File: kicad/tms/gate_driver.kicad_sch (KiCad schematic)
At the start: 12 parts, among them T2 Transformer_1P_1S, U4 L7812, U5 TC4420, U6 NSL-32

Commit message: Kicad files
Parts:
- removed C4: 0.33μF, symbol Device:C
- removed C5: 0.1μF, symbol Device:C
- removed U4: L7812, symbol Regulator_Linear:L7812
- T2: value Transformer_1P_1S -> P0584NL
- U5: renamed from U6; value NSL-32 -> VO2611
- renumbered C9 to C8, C6 to C9, R11 to R18, R12 to R19, U5 to U6
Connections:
- net PSU 12V: now reaches C8.1, C9.1, U6.1 (VDD), U6.8 (VDD)
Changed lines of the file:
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@@
     (title "Gate Driver Circuit")
   )
-  (junction (at 106.68 95.25) (diameter 0) (color 0 0 0 0)
-  )
-  (junction (at 115.57 87.63) (diameter 0) (color 0 0 0 0)
-  )
-  (junction (at 97.79 87.63) (diameter 0) (color 0 0 0 0)
-  )
   (junction (at 207.01 96.52) (diameter 0) (color 0 0 0 0)
   )
@@
     (stroke (width 0) (type default))
   )
-  (wire (pts (xy 97.79 95.25) (xy 106.68 95.25))
-    (stroke (width 0) (type default))
-  )
   (wire (pts (xy 130.81 109.22) (xy 116.84 109.22))
     (stroke (width 0) (type default))
@@
     (stroke (width 0) (type default))
   )
-  (wire (pts (xy 83.82 87.63) (xy 97.79 87.63))
-    (stroke (width 0) (type default))
-  )
   (wire (pts (xy 158.75 87.63) (xy 157.48 87.63))
     (stroke (width 0) (type default))
   )
-  (wire (pts (xy 114.3 87.63) (xy 115.57 87.63))
-    (stroke (width 0) (type default))
-  )
   (wire (pts (xy 207.01 97.79) (xy 207.01 96.52))
     (stroke (width 0) (type default))
   )
-  (wire (pts (xy 106.68 95.25) (xy 115.57 95.25))
-    (stroke (width 0) (type default))
-  )
-  (wire (pts (xy 97.79 87.63) (xy 99.06 87.63))
-    (stroke (width 0) (type default))
-  )
   (wire (pts (xy 158.75 87.63) (xy 158.75 104.14))
     (stroke (width 0) (type default))
@@
     (stroke (width 0) (type default))
   )
-  (wire (pts (xy 115.57 87.63) (xy 143.51 87.63))
+  (wire (pts (xy 135.89 87.63) (xy 143.51 87.63))
     (stroke (width 0) (type default))
   )
@@
     )
   )
-  (global_label "PSU 24V" (shape input) (at 83.82 87.63 180) (fields_autoplaced)
+  (global_label "PSU 12V" (shape input) (at 135.89 87.63 180) (fields_autoplaced)
     (effects (font (size 1.27 1.27)) (justify right))
-    (property "Intersheetrefs" "${INTERSHEET_REFS}" (at 72.5496 87.63 0)
+    (property "Intersheetrefs" "${INTERSHEET_REFS}" (at 124.6196 87.63 0)
       (effects (font (size 1.27 1.27)) (justify right) hide)
     )
@@
     )
   )
-  (symbol (lib_id "Device:C") (at 97.79 91.44 0) (mirror y) (unit 1)
-    (in_bom yes) (on_board yes) (dnp no)
-    (property "Reference" "C4" (at 93.98 90.17 0)
-      (effects (font (size 1.27 1.27)) (justify left))
-    )
-    (property "Value" "0.33μF" (at 93.98 92.71 0)
-      (effects (font (size 1.27 1.27)) (justify left))
-    )
-    (property "Footprint" "" (at 96.8248 95.25 0)
-      (effects (font (size 1.27 1.27)) hide)
-    )
-    (property "Datasheet" "~" (at 97.79 91.44 0)
-      (effects (font (size 1.27 1.27)) hide)
-    )
-    (pin "1")
-    (pin "2")
-    (instances
-      (project "tms"
-        (path "/dc88686f-c772-4c63-b1cc-83a281c6b46c/025e288f-ab42-4019-86f4-e6a324d46d8a"
-          (reference "C4") (unit 1)
-        )
-      )
-    )
-  )
   (symbol (lib_id "power:+5V") (at 97.79 109.22 0) (unit 1)
     (in_bom yes) (on_board yes) (dnp no)
@@
         (path "/dc88686f-c772-4c63-b1cc-83a281c6b46c/025e288f-ab42-4019-86f4-e6a324d46d8a"
           (reference "#PWR011") (unit 1)
-        )
-      )
-    )
-  )
-  (symbol (lib_id "Regulator_Linear:L7812") (at 106.68 87.63 0) (unit 1)
-    (in_bom yes) (on_board yes) (dnp no) (fields_autoplaced)
-    (property "Reference" "U4" (at 106.68 81.28 0)
-      (effects (font (size 1.27 1.27)))
-    )
-    (property "Value" "L7812" (at 106.68 83.82 0)
-      (effects (font (size 1.27 1.27)))
-    )
-    (property "Footprint" "" (at 107.315 91.44 0)
-      (effects (font (size 1.27 1.27) italic) (justify left) hide)
-    )
-    (property "Datasheet" "http://www.st.com/content/ccc/resource/technical/document/datasheet/41/4f/b3/b0/12/d4/47/88/CD00000444.pdf/files/CD00000444.pdf/jcr:content/translations/en.CD00000444.pdf" (at 106.68 88.9 0)
-      (effects (font (size 1.27 1.27)) hide)
-    )
-    (pin "1")
-    (pin "3")
-    (pin "2")
-    (instances
-      (project "tms"
-        (path "/dc88686f-c772-4c63-b1cc-83a281c6b46c/025e288f-ab42-4019-86f4-e6a324d46d8a"
-          (reference "U4") (unit 1)
         )
       )
@@
     )
   )
-  (symbol (lib_id "power:GND") (at 106.68 95.25 0) (unit 1)
-    (in_bom yes) (on_board yes) (dnp no) (fields_autoplaced)
-    (property "Reference" "#PWR09" (at 106.68 101.6 0)
-      (effects (font (size 1.27 1.27)) hide)
-    )
-    (property "Value" "GND" (at 106.68 100.33 0)
-      (effects (font (size 1.27 1.27)))
-    )
-    (property "Footprint" "" (at 106.68 95.25 0)
-      (effects (font (size 1.27 1.27)) hide)
-    )
-    (property "Datasheet" "" (at 106.68 95.25 0)
-      (effects (font (size 1.27 1.27)) hide)
-    )
-    (pin "1")
-    (instances
-      (project "tms"
-        (path "/dc88686f-c772-4c63-b1cc-83a281c6b46c/025e288f-ab42-4019-86f4-e6a324d46d8a"
-          (reference "#PWR09") (unit 1)
-        )
-      )
-    )
-  )
   (symbol (lib_id "Isolator:NSL-32") (at 114.3 116.84 90) (unit 1)
     (in_bom yes) (on_board yes) (dnp no) (fields_autoplaced)
-    (property "Reference" "U6" (at 119.38 115.57 90)
+    (property "Reference" "U5" (at 119.38 115.57 90)
       (effects (font (size 1.27 1.27)) (justify right))
     )
-    (property "Value" "NSL-32" (at 119.38 118.11 90)
+    (property "Value" "VO2611" (at 119.38 118.11 90)
       (effects (font (size 1.27 1.27)) (justify right))
     )
@@
       (project "tms"
         (path "/dc88686f-c772-4c63-b1cc-83a281c6b46c/025e288f-ab42-4019-86f4-e6a324d46d8a"
-          (reference "U6") (unit 1)
+          (reference "U5") (unit 1)
         )
       )
@@
   (symbol (lib_id "Device:R") (at 104.14 109.22 90) (mirror x) (unit 1)
     (in_bom yes) (on_board yes) (dnp no)
-    (property "Reference" "R11" (at 104.14 115.57 90)
+    (property "Reference" "R18" (at 104.14 115.57 90)
       (effects (font (size 1.27 1.27)))
     )
@@
       (project "tms"
         (path "/dc88686f-c772-4c63-b1cc-83a281c6b46c/025e288f-ab42-4019-86f4-e6a324d46d8a"
-          (reference "R11") (unit 1)
+          (reference "R18") (unit 1)
         )
       )
@@
   (symbol (lib_id "Device:C") (at 153.67 87.63 90) (unit 1)
     (in_bom yes) (on_board yes) (dnp no)
-    (property "Reference" "C6" (at 153.67 81.28 90)
+    (property "Reference" "C9" (at 153.67 81.28 90)
       (effects (font (size 1.27 1.27)))
     )
@@
       (project "tms"
         (path "/dc88686f-c772-4c63-b1cc-83a281c6b46c/025e288f-ab42-4019-86f4-e6a324d46d8a"
-          (reference "C6") (unit 1)
+          (reference "C9") (unit 1)
         )
       )
@@
     )
   )
-  (symbol (lib_id "Device:C") (at 115.57 91.44 0) (unit 1)
-    (in_bom yes) (on_board yes) (dnp no)
-    (property "Reference" "C5" (at 119.38 90.17 0)
-      (effects (font (size 1.27 1.27)) (justify left))
-    )
-    (property "Value" "0.1μF" (at 119.38 92.71 0)
-      (effects (font (size 1.27 1.27)) (justify left))
-    )
-    (property "Footprint" "" (at 116.5352 95.25 0)
-      (effects (font (size 1.27 1.27)) hide)
-    )
-    (property "Datasheet" "~" (at 115.57 91.44 0)
-      (effects (font (size 1.27 1.27)) hide)
-    )
-    (pin "1")
-    (pin "2")
-    (instances
-      (project "tms"
-        (path "/dc88686f-c772-4c63-b1cc-83a281c6b46c/025e288f-ab42-4019-86f4-e6a324d46d8a"
-          (reference "C5") (unit 1)
-        )
-      )
-    )
-  )
   (symbol (lib_id "power:GND") (at 143.51 104.14 0) (unit 1)
     (in_bom yes) (on_board yes) (dnp no) (fields_autoplaced)
@@
   (symbol (lib_id "Device:C") (at 153.67 76.2 90) (unit 1)
     (in_bom yes) (on_board yes) (dnp no)
-    (property "Reference" "C9" (at 153.67 69.85 90)
+    (property "Reference" "C8" (at 153.67 69.85 90)
       (effects (font (size 1.27 1.27)))
     )
@@
       (project "tms"
         (path "/dc88686f-c772-4c63-b1cc-83a281c6b46c/025e288f-ab42-4019-86f4-e6a324d46d8a"
-          (reference "C9") (unit 1)
+          (reference "C8") (unit 1)
         )
       )
@@
   (symbol (lib_id "Driver_FET:TC4422") (at 143.51 96.52 0) (unit 1)
     (in_bom yes) (on_board yes) (dnp no)
-    (property "Reference" "U5" (at 143.51 83.82 0)
+    (property "Reference" "U6" (at 143.51 83.82 0)
       (effects (font (size 1.27 1.27)))
     )
@@
       (project "tms"
         (path "/dc88686f-c772-4c63-b1cc-83a281c6b46c/025e288f-ab42-4019-86f4-e6a324d46d8a"
-          (reference "U5") (unit 1)
+          (reference "U6") (unit 1)
         )
       )
@@
   (symbol (lib_id "Device:R") (at 199.39 96.52 90) (unit 1)
     (in_bom yes) (on_board yes) (dnp no) (fields_autoplaced)
-    (property "Reference" "R12" (at 199.39 90.17 90)
+    (property "Reference" "R19" (at 199.39 90.17 90)
       (effects (font (size 1.27 1.27)))
     )
@@
       (project "tms"
         (path "/dc88686f-c772-4c63-b1cc-83a281c6b46c/025e288f-ab42-4019-86f4-e6a324d46d8a"
-          (reference "R12") (unit 1)
+          (reference "R19") (unit 1)
         )
       )
@@
       (effects (font (size 1.27 1.27)))
     )
-    (property "Value" "Transformer_1P_1S" (at 172.7327 93.98 0)
-      (effects (font (size 1.27 1.27)))
-    )
+    (property "Value" "P0584NL" (at 172.7327 93.98 0)
+      (effects (font (size 1.27 1.27)))
+    )

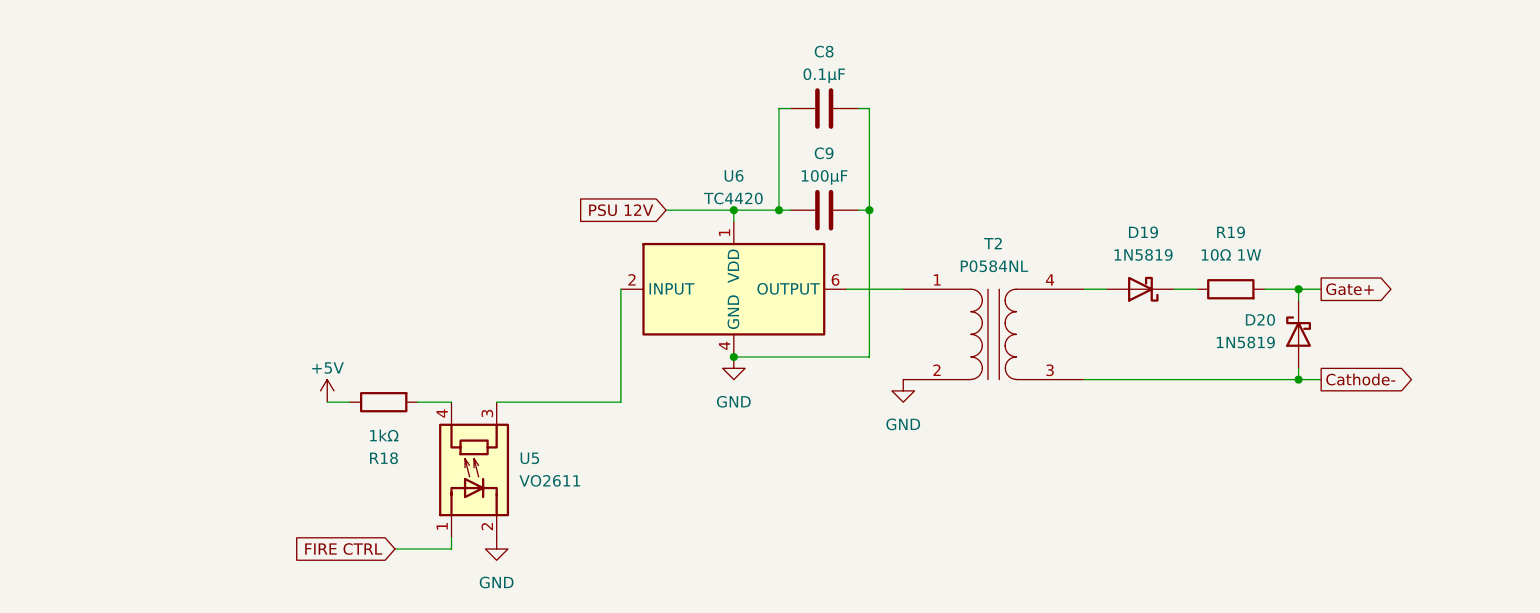
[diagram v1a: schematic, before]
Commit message: Schematic fixes after real life tests
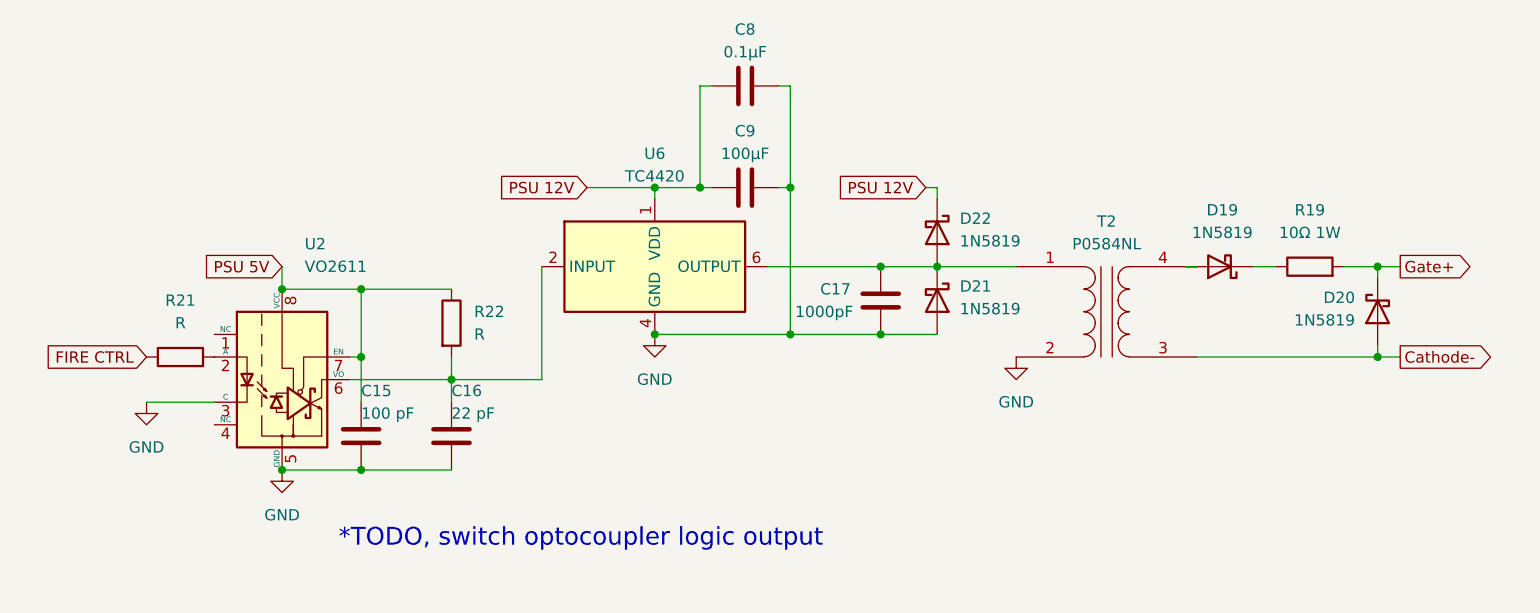
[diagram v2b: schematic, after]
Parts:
- removed R18: 1kΩ, symbol Device:R
- removed U5: VO2611, OptoDevice:Luna_NSL-32, symbol Isolator:NSL-32
- added C15: 100 pF, symbol Device:C
- added C16: 22 pF, symbol Device:C
- added C17: 1000pF, symbol Device:C
- added D21, D22: 1N5819, symbol Device:D_Schottky
- added R21, R22: R, symbol Device:R
- added U2: VO2611, Package_DIP:DIP-8_W7.62mm, symbol Isolator:VO2611
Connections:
- net FIRE CTRL: now also R21.1
- net GND: now also C15.2, C16.2, C17.2, D21.2 (A), U2.3 (C), U2.5 (GND)
- net PSU 12V: now also D22.1 (K)
- net at U6.2 (INPUT): now also C16.1, R22.2, U2.6 (VO)
- net at T2.1 (AA), U6.6 (OUTPUT), U6.7 (OUTPUT): now also C17.1, D21.1 (K), D22.2 (A)
- new net: R21.2, U2.2 (A)
- new net PSU 5V: C15.1, R22.1, U2.7 (EN), U2.8 (VCC)
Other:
- note added: "*TODO, switch optocoupler logic output"
- moved on the sheet: C8, C9, D19, D20, R19, T2, U6

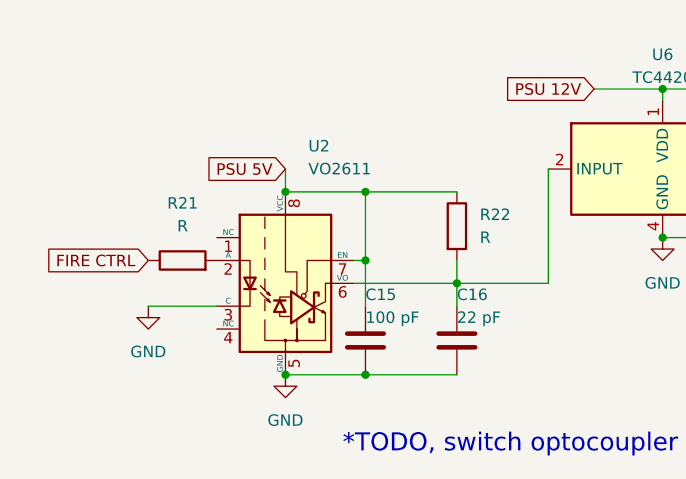
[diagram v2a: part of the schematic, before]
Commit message: Fixed optocoupler output logic
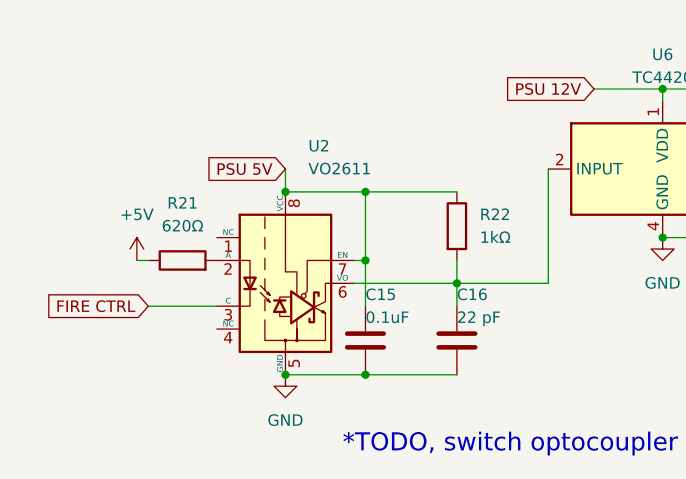
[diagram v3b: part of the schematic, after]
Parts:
- C15: value 100 pF -> 0.1uF
- R21: value R -> 620Ω
- R22: value R -> 1kΩ
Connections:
- net FIRE CTRL: now also U2.3 (C); no longer R21.1
- net GND: no longer U2.3 (C)
- new net +5V: R21.1
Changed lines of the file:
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@@
+    (stroke (width 0) (type default))
+  )
+  (wire (pts (xy 76.2 104.14) (xy 77.47 104.14))
     (stroke (width 0) (type default))
   )
@@
     )
   )
-  (global_label "FIRE CTRL" (shape input) (at 77.47 104.14 180) (fields_autoplaced)
+  (global_label "FIRE CTRL" (shape input) (at 77.47 109.22 180) (fields_autoplaced)
     (effects (font (size 1.27 1.27)) (justify right))
-    (property "Intersheetrefs" "${INTERSHEET_REFS}" (at 64.8691 104.14 0)
+    (property "Intersheetrefs" "${INTERSHEET_REFS}" (at 64.8691 109.22 0)
       (effects (font (size 1.27 1.27)) (justify right) hide)
+    )
+  )
+  (symbol (lib_id "power:+5V") (at 76.2 104.14 0) (unit 1)
+    (in_bom yes) (on_board yes) (dnp no) (fields_autoplaced)
+    (property "Reference" "#PWR012" (at 76.2 107.95 0)
+      (effects (font (size 1.27 1.27)) hide)
+    )
+    (property "Value" "+5V" (at 76.2 99.06 0)
+      (effects (font (size 1.27 1.27)))
+    )
+    (property "Footprint" "" (at 76.2 104.14 0)
+      (effects (font (size 1.27 1.27)) hide)
+    )
+    (property "Datasheet" "" (at 76.2 104.14 0)
+      (effects (font (size 1.27 1.27)) hide)
+    )
+    (pin "1")
+    (instances
+      (project "tms"
+        (path "/dc88686f-c772-4c63-b1cc-83a281c6b46c/025e288f-ab42-4019-86f4-e6a324d46d8a"
+          (reference "#PWR012") (unit 1)
+        )
+      )
     )
   )
@@
       (effects (font (size 1.27 1.27)) (justify left))
     )
-    (property "Value" "R" (at 114.3 101.6 0)
+    (property "Value" "1kΩ" (at 114.3 101.6 0)
       (effects (font (size 1.27 1.27)) (justify left))
     )
@@
     )
   )
-  (symbol (lib_id "power:GND") (at 77.47 109.22 0) (unit 1)
-    (in_bom yes) (on_board yes) (dnp no) (fields_autoplaced)
-    (property "Reference" "#PWR016" (at 77.47 115.57 0)
-      (effects (font (size 1.27 1.27)) hide)
-    )
-    (property "Value" "GND" (at 77.47 114.3 0)
-      (effects (font (size 1.27 1.27)))
-    )
-    (property "Footprint" "" (at 77.47 109.22 0)
-      (effects (font (size 1.27 1.27)) hide)
-    )
-    (property "Datasheet" "" (at 77.47 109.22 0)
-      (effects (font (size 1.27 1.27)) hide)
-    )
-    (pin "1")
-    (instances
-      (project "tms"
-        (path "/dc88686f-c772-4c63-b1cc-83a281c6b46c/025e288f-ab42-4019-86f4-e6a324d46d8a"
-          (reference "#PWR016") (unit 1)
-        )
-      )
-    )
-  )
   (symbol (lib_id "Device:C") (at 144.78 73.66 90) (unit 1)
     (in_bom yes) (on_board yes) (dnp no)
@@
       (effects (font (size 1.27 1.27)))
     )
-    (property "Value" "R" (at 81.28 100.33 90)
+    (property "Value" "620Ω" (at 81.28 100.33 90)
       (effects (font (size 1.27 1.27)))
     )
@@
       (effects (font (size 1.27 1.27)) (justify left))
     )
-    (property "Value" "100 pF" (at 101.6 110.49 0)
-      (effects (font (size 1.27 1.27)) (justify left))
-    )
+    (property "Value" "0.1uF" (at 101.6 110.49 0)
+      (effects (font (size 1.27 1.27)) (justify left))
+    )

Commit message: Fixed TMS schematic
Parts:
- R29: renamed from R22; value 1kΩ -> 1.2kΩ
- R30: renamed from R19; value 10Ω 1W -> 10Ω
- renumbered C15 to C16, C16 to C17, C8 to C18, C9 to C19, C17 to C20, D21 to D19, D22 to D20, D19 to D21, D20 to D22, R21 to R28, U2 to U10, U6 to U11
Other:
- note removed: "*TODO, switch optocoupler logic output"

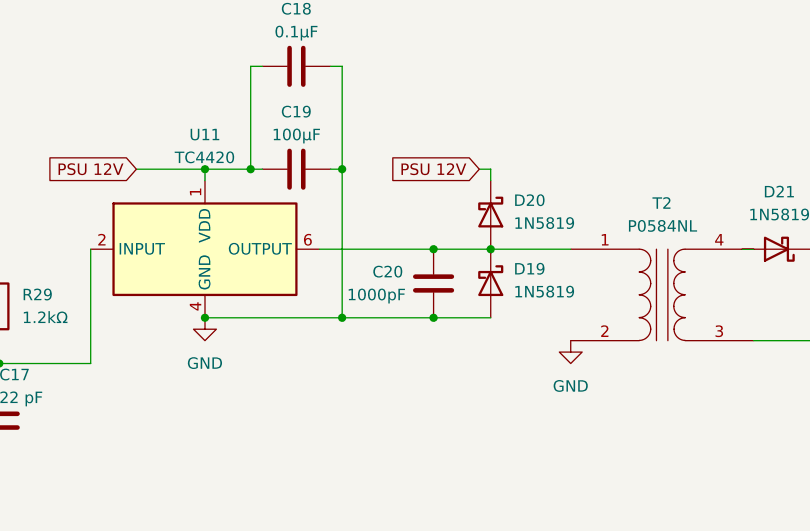
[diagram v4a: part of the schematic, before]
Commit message: Schematic changes
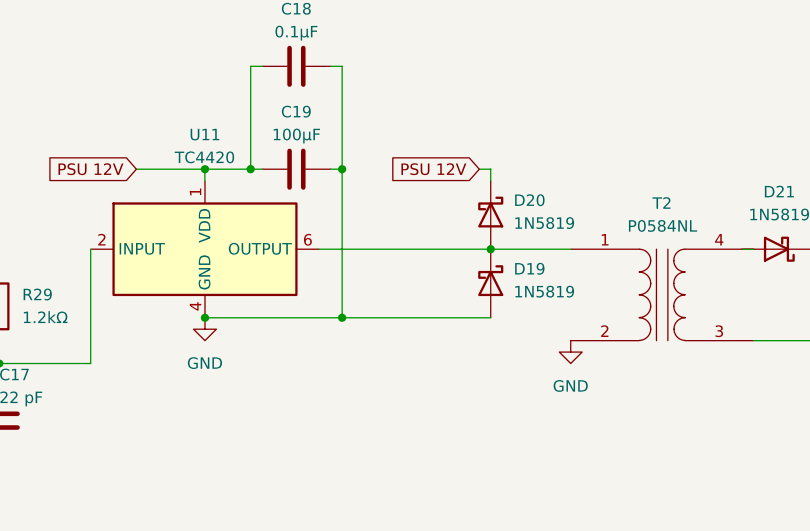
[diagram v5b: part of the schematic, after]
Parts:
- removed C20: 1000pF, symbol Device:C
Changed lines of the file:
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@@
   (junction (at 134.62 85.09) (diameter 0) (color 0 0 0 0)
   )
-  (junction (at 160.02 93.98) (diameter 0) (color 0 0 0 0)
-  )
   (junction (at 111.76 106.68) (diameter 0) (color 0 0 0 0)
   )
@@
   (junction (at 101.6 104.14) (diameter 0) (color 0 0 0 0)
   )
-  (junction (at 160.02 101.6) (diameter 0) (color 0 0 0 0)
-  )
   (junction (at 149.86 85.09) (diameter 0) (color 0 0 0 0)
   )
@@
     (stroke (width 0) (type default))
   )
-  (wire (pts (xy 149.86 101.6) (xy 160.02 101.6))
+  (wire (pts (xy 149.86 101.6) (xy 166.37 101.6))
     (stroke (width 0) (type default))
   )
@@
     (stroke (width 0) (type default))
   )
-  (wire (pts (xy 160.02 93.98) (xy 166.37 93.98))
-    (stroke (width 0) (type default))
-  )
   (wire (pts (xy 215.9 93.98) (xy 218.44 93.98))
     (stroke (width 0) (type default))
@@
     (stroke (width 0) (type default))
   )
-  (wire (pts (xy 147.32 93.98) (xy 160.02 93.98))
+  (wire (pts (xy 147.32 93.98) (xy 166.37 93.98))
     (stroke (width 0) (type default))
   )
@@
   )
   (wire (pts (xy 195.58 104.14) (xy 215.9 104.14))
-    (stroke (width 0) (type default))
-  )
-  (wire (pts (xy 160.02 101.6) (xy 166.37 101.6))
     (stroke (width 0) (type default))
   )
@@
         )
       )
-    )
-  )
-  (symbol (lib_id "Device:C") (at 160.02 97.79 0) (mirror y) (unit 1)
-    (in_bom yes) (on_board yes) (dnp no)
-    (property "Reference" "C20" (at 154.94 96.52 0)
-      (effects (font (size 1.27 1.27)))
-    )
-    (property "Value" "1000pF" (at 153.67 99.06 0)
-      (effects (font (size 1.27 1.27)))
-    )
-    (property "Footprint" "" (at 159.0548 101.6 0)
-      (effects (font (size 1.27 1.27)) hide)
-    )
-    (property "Datasheet" "~" (at 160.02 97.79 0)
-      (effects (font (size 1.27 1.27)) hide)
-    )
-    (pin "1")
-    (pin "2")
-    (instances
-      (project "tms"
-        (path "/dc88686f-c772-4c63-b1cc-83a281c6b46c/025e288f-ab42-4019-86f4-e6a324d46d8a"
-          (reference "C20") (unit 1)
-        )
-      )
